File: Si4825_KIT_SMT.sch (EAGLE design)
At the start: 26 parts, among them U1 SI4825, U2 LMV358SOIC, Y1 32.768kHz

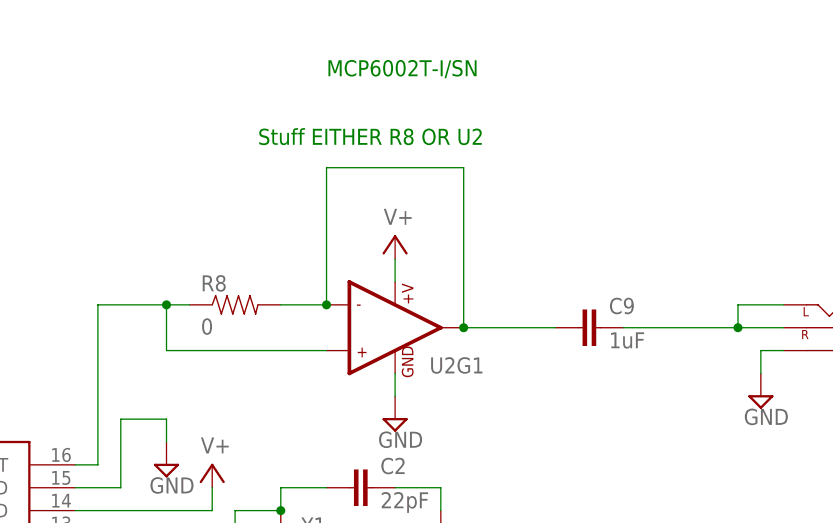
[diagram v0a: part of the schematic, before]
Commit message: Fixed issues discovered in first build
- fixed potentiometer footprint
- bigger strain relief holes: .1” to .15”
- changed value of C9 (AC coupling capacitor) to 22uF in BOM and
schematic
- Removed R8 (jumper to bypass op amp)
- Increased length of surface mount pads for 0805 components to
facilitate hand soldering
- Regenerated gerbers, jpg previews, and pdf of schematic
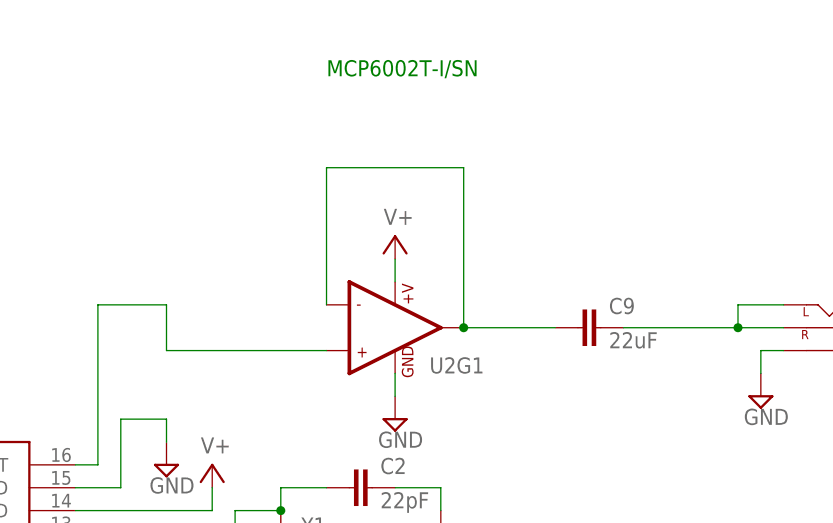
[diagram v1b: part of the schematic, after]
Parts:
- removed R8: 0, SparkFun-Resistors:RESISTOR0805-RES
- C9: value 1uF -> 22uF
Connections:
- net N$14: no longer R8.1
- net N$17: no longer R8.2
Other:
- note removed: "Stuff EITHER R8 OR U2"
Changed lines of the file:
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@@
 <setting verticaltext="up"/>
 </settings>
-<grid distance="0.1" unitdist="inch" unit="inch" style="lines" multiple="1" display="no" altdistance="0.05" altunitdist="inch" altunit="inch"/>
+<grid distance="0.1" unitdist="inch" unit="inch" style="lines" multiple="1" display="no" altdistance="0.01" altunitdist="inch" altunit="inch"/>
 <layers>
 <layer number="1" name="Top" color="4" fill="1" visible="no" active="no"/>
@@
 <part name="SUPPLY19" library="supply2" deviceset="V+" device=""/>
 <part name="C8" library="SparkFun-Passives" deviceset="CAP" device="0805" value="1uF"/>
-<part name="C9" library="SparkFun-Passives" deviceset="CAP" device="0805" value="1uF"/>
-<part name="R8" library="SparkFun-Resistors" deviceset="RESISTOR" device="0805-RES" value="0"/>
+<part name="C9" library="SparkFun-Passives" deviceset="CAP" device="0805" value="22uF"/>
 </parts>
 <sheets>
@@
 <text x="20.32" y="101.6" size="1.778" layer="91">Diodes Incorporated S1A-13-F or equiv</text>
 <text x="111.76" y="99.06" size="1.778" layer="91">MCP6002T-I/SN</text>
-<text x="104.14" y="91.44" size="1.778" layer="91">Stuff EITHER R8 OR U2</text>
 </plain>
 <instances>
@@
 <attribute name="VALUE" x="143.129" y="68.834" size="1.778" layer="96"/>
 </instance>
-<instance part="R8" gate="G$1" x="101.6" y="73.66"/>
 </instances>
 <busses>
@@
 <pinref part="U1" gate="G$1" pin="AOUT"/>
 <wire x1="86.36" y1="55.88" x2="83.82" y2="55.88" width="0.1524" layer="91"/>
-<pinref part="R8" gate="G$1" pin="1"/>
 <wire x1="86.36" y1="73.66" x2="93.98" y2="73.66" width="0.1524" layer="91"/>
-<wire x1="93.98" y1="73.66" x2="96.52" y2="73.66" width="0.1524" layer="91"/>
 <wire x1="93.98" y1="73.66" x2="93.98" y2="68.58" width="0.1524" layer="91"/>
-<junction x="93.98" y="73.66"/>
 <pinref part="U2" gate="G1" pin="+IN1"/>
 <wire x1="93.98" y1="68.58" x2="111.76" y2="68.58" width="0.1524" layer="91"/>
@@
 <pinref part="U2" gate="G1" pin="-IN1"/>
 <wire x1="111.76" y1="88.9" x2="111.76" y2="73.66" width="0.1524" layer="91"/>
-<pinref part="R8" gate="G$1" pin="2"/>
-<wire x1="106.68" y1="73.66" x2="111.76" y2="73.66" width="0.1524" layer="91"/>
-<junction x="111.76" y="73.66"/>
 <pinref part="U2" gate="G1" pin="OUT1"/>
 <wire x1="127" y1="88.9" x2="127" y2="71.12" width="0.1524" layer="91"/>
